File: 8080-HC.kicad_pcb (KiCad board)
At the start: 4 copper layers, 352 parts, among them U1 74HCU04, U10 74HC00, U11 74HC126, U12 74HC161, U13 74HC238, U14 74HC238, U15 74HC238, U16 74HC238, U17 74HC04, U178 74LS03, U18 74HC05, U181 74HC244, U182 74HC244, U19 74HC74, U194 74HC244, U195 74HC244, U2 74HC74, U20 74HC373, U21 74HC373, U215 74HC193, U216 74HC193, U217 74HC193, U218 74HC193, U22 74HC373, U23 74HC373, U231 74HC245, U232 74HC04, U233 74HC04, U234 74LS373, U239 74HC74, U24 74HC373, U242 74HC00, U243 74HCU04, U244 74HC00, U25 74HC244, U26 74HC244, U27 74HC244, U28 74HC244, U29 74HC244, U3 74HC00, U30 74HC373, U31 74HC373, U32 74HC244, U33 74HC244, U34 74HC244, U35 74HC244, U36 74HC373, U37 74HC373, U38 74HC244, U39 74HC244, U4 74HC04, U40 74HC244, U41 74HC244, U43 74HC04, U44 74HC04, U46 74HC04, U47 74HC04, U48 74HC04, U49 74HC04, U5 74HC00, U50 74HC04, U51 74HC04, U52 74HC04, U53 74HC238, U54 74HC238, U55 74HC238, U56 74HC238, U57 74HC04, U58 74HC04, U6 74HC04, U69 74HC05, U7 74HC05, U70 74LS05, U71 74HC04, U72 74LS126, U73 74LS126, U74 74LS126, U75 74LS126, U76 74LS126, U77 74HC00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

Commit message: place u229, u230 and D0-D7 leds
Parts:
- added U229: 74HC04, Package_DIP:DIP-14_W7.62mm, F.Cu at (-284.5, -30.5)
- added U230: 74HC04, Package_DIP:DIP-14_W7.62mm, F.Cu at (-261.6, -30.5)
- added U43: 74HC04, Package_DIP:DIP-14_W7.62mm, F.Cu at (-66.0, -45.7)
- moved L250 362.4 mm to (-249.7, -6.35), turned to 90 degrees
- moved L248 362.1 mm to (-258.8, -6.35), turned to 90 degrees
- moved L253 353.3 mm to (-236.0, -6.35), turned to 90 degrees
- moved L247 338.7 mm to (-263.4, -6.35), turned to 90 degrees
- moved L246 337.1 mm to (-268.0, -6.35), turned to 90 degrees
- moved L251 319.5 mm to (-245.1, -6.35), turned to 90 degrees
- moved B35 314.8 mm to (-236.2, -14.0), turned to 180 degrees
- moved L249 303.4 mm to (-254.3, -6.35), turned to 90 degrees
- moved L252 302.1 mm to (-240.5, -6.35), turned to 90 degrees
- renumbered D102 to L246, D100 to L247, D98 to L248, D96 to L249, D94 to L250, D92 to L251, D90 to L252, D89 to L253
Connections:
- L246 pad 1: Net-(D102-Pad1) -> Net-(L246-Pad1)
- L247 pad 1: Net-(D100-Pad1) -> Net-(L247-Pad1)
- L248 pad 1: Net-(D98-Pad1) -> Net-(L248-Pad1)
- L249 pad 1: Net-(D96-Pad1) -> Net-(L249-Pad1)
- L250 pad 1: Net-(D94-Pad1) -> Net-(L250-Pad1)
- L251 pad 1: Net-(D92-Pad1) -> Net-(L251-Pad1)
- L252 pad 1: Net-(D90-Pad1) -> Net-(L252-Pad1)
- L253 pad 1: Net-(D89-Pad1) -> Net-(L253-Pad1)
- U17 pad 10: Net-(D96-Pad1) -> (no net)
- U17 pad 11: io_D4 -> (no net)
- U17 pad 14: VCC -> (no net)
- U17 pad 5: io_D2 -> (no net)
- U17 pad 6: Net-(D92-Pad1) -> (no net)
- U17 pad 7: GND -> (no net)
- U17 pad 8: Net-(D94-Pad1) -> (no net)
- U17 pad 9: io_D3 -> (no net)
- U4 pad 1: io_D0 -> (no net)
- U4 pad 14: VCC -> (no net)
- U4 pad 2: Net-(D89-Pad1) -> (no net)
- U4 pad 3: io_D1 -> (no net)
- U4 pad 4: Net-(D90-Pad1) -> (no net)
- U4 pad 7: GND -> (no net)
- U6 pad 12: Net-(D98-Pad1) -> (no net)
- U6 pad 13: io_D5 -> (no net)

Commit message: address display leds set and half routed
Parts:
- removed the U43 at (-66.0, -45.7)
- removed the U43 at (-162.6, -295.8)
- removed U46: 74HC04, Package_DIP:DIP-14_W7.62mm
- removed the U49 at (-121.0, -302.6)
- added U228: 74HC04, Package_DIP:DIP-14_W7.62mm, F.Cu at (-312.4, -30.5)
- added U43: 74HC04, Package_DIP:DIP-14_W7.62mm, F.Cu at (-378.5, -45.0)
- added U47: 74HC04, Package_DIP:DIP-14_W7.62mm, F.Cu at (-356.8, -45.0)
- B1: renamed from RN19; value R_Network08 -> 1K
- B3: renamed from RN20; value R_Network08 -> 1K
- B33: renamed from RN16; value R_Network08 -> 2.2K
- B34: renamed from RN14; value R_Network08 -> 2.2K
- B43: renamed from RN10; value R_Network08 -> 1K
- B44: renamed from RN12; value R_Network08 -> 1K
- moved B44 436.4 mm to (-264.2, 108.7), turned to 90 degrees
- moved B43 419.1 mm to (-264.2, 83.9), turned to 90 degrees
- moved U44 385.3 mm to (-367.6, -45.0)
- moved L234 384.7 mm to (-327.4, -6.35), turned to 90 degrees
- moved L241 373.4 mm to (-294.1, -6.35), turned to 90 degrees
- moved L243 372.8 mm to (-285.0, -6.35), turned to 90 degrees
- moved L231 372.4 mm to (-341.1, -6.35), turned to 90 degrees
- moved L230 366.9 mm to (-345.7, -6.35), turned to 90 degrees
- moved L238 355.3 mm to (-307.8, -6.35), turned to 90 degrees
- moved L233 354.9 mm to (-332.0, -6.35), turned to 90 degrees
- moved L237 350.9 mm to (-313.7, -6.35), turned to 90 degrees
- moved L240 349.9 mm to (-298.7, -6.35), turned to 90 degrees
- moved L244 344.4 mm to (-280.4, -6.35), turned to 90 degrees
- moved B34 339.8 mm to (-275.8, -14.0), turned to 180 degrees
- moved L235 339.6 mm to (-322.8, -6.35), turned to 90 degrees
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- renumbered D122 to L230, D119 to L231, D116 to L232, D113 to L233, D110 to L234, D108 to L235, D106 to L236, D105 to L237, D104 to L238, D103 to L239, D101 to L240, D99 to L241, D97 to L242, D95 to L243, D93 to L244, D91 to L245, U47 to U227
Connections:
- B38 pad 2: Net-(B38-Pad2) -> (no net)
- B38 pad 3: Net-(B38-Pad3) -> (no net)
- B38 pad 4: Net-(B38-Pad4) -> (no net)
- B38 pad 5: Net-(B38-Pad5) -> (no net)
- B38 pad 8: Net-(B38-Pad8) -> (no net)
- B38 pad 9: Net-(B38-Pad9) -> (no net)
- B43 pad 2: /I/O regs/A15 -> A15
- B43 pad 3: /I/O regs/A14 -> A14
- B43 pad 4: /I/O regs/A13 -> A13
- B43 pad 5: /I/O regs/A12 -> A12
- B43 pad 6: /I/O regs/A11 -> A11
- B43 pad 7: /I/O regs/A10 -> A10
- B43 pad 8: /I/O regs/A9 -> A9
- B43 pad 9: /I/O regs/A8 -> A8
- B44 pad 2: /I/O regs/A7 -> A7
- B44 pad 3: /I/O regs/A6 -> A6
- B44 pad 4: /I/O regs/A5 -> A5
- B44 pad 5: /I/O regs/A4 -> A4
- B44 pad 6: /I/O regs/A3 -> A3
- B44 pad 7: /I/O regs/A2 -> A2
- B44 pad 8: /I/O regs/A1 -> A1
- B44 pad 9: /I/O regs/A0 -> A0
- L218 pad 1: Net-(L218-Pad1) -> (no net)
- L230 pad 1: Net-(D122-Pad1) -> Net-(L230-Pad1)
- L231 pad 1: Net-(D119-Pad1) -> Net-(L231-Pad1)
- L232 pad 1: Net-(D116-Pad1) -> Net-(L232-Pad1)
- L233 pad 1: Net-(D113-Pad1) -> Net-(L233-Pad1)
- L234 pad 1: Net-(D110-Pad1) -> Net-(L234-Pad1)
- L235 pad 1: Net-(D108-Pad1) -> Net-(L235-Pad1)
- L238 pad 1: Net-(D104-Pad1) -> Net-(L238-Pad1)
- L239 pad 1: Net-(D103-Pad1) -> Net-(L239-Pad1)
- L242 pad 1: Net-(D97-Pad1) -> Net-(L242-Pad1)
- L243 pad 1: Net-(D95-Pad1) -> Net-(L243-Pad1)
- L244 pad 1: Net-(D93-Pad1) -> Net-(L244-Pad1)
- L245 pad 1: Net-(D91-Pad1) -> Net-(L245-Pad1)
- L277 pad 1: BUSAK -> (no net)
- U10 pad 10: Net-(U10-Pad10) -> (no net)
- U10 pad 11: Net-(U10-Pad11) -> (no net)
- U10 pad 12: Net-(U10-Pad12) -> (no net)
- U10 pad 13: Net-(U10-Pad13) -> (no net)
- U10 pad 8: Net-(U10-Pad8) -> (no net)
- U10 pad 9: Net-(U10-Pad9) -> (no net)
- U11 pad 1: Net-(U11-Pad1) -> (no net)
- U11 pad 11: /Timings Generator/QC -> (no net)
- U11 pad 3: /Timings Generator/QA -> (no net)
- U11 pad 6: /Timings Generator/QB -> (no net)
- U11 pad 8: /Timings Generator/QD -> (no net)
- U12 pad 2: /Timings Generator/CLK -> (no net)
- U13 pad 10: Net-(U13-Pad10) -> (no net)
- U13 pad 11: Net-(U13-Pad11) -> (no net)
- U13 pad 12: Net-(U13-Pad12) -> (no net)
- U13 pad 13: /Timings Generator/W2 -> (no net)
- U13 pad 14: /Timings Generator/W1 -> (no net)
- U13 pad 15: /Timings Generator/W0 -> (no net)
- U13 pad 7: Net-(U13-Pad7) -> (no net)
- U13 pad 9: Net-(U13-Pad9) -> (no net)
- U14 pad 10: Net-(U14-Pad10) -> (no net)
- U14 pad 11: Net-(U14-Pad11) -> (no net)
- U14 pad 12: Net-(U14-Pad12) -> (no net)
- U14 pad 13: /Timings Generator/M2 -> (no net)
- U14 pad 14: Net-(U14-Pad14) -> (no net)
- U14 pad 15: Net-(U14-Pad15) -> (no net)
- U14 pad 7: Net-(U14-Pad7) -> (no net)
- U14 pad 9: Net-(U14-Pad9) -> (no net)
- U15 pad 10: Net-(U15-Pad10) -> (no net)
- U15 pad 11: /Timings Generator/T12 -> (no net)
- U15 pad 12: Net-(U15-Pad12) -> (no net)
- U15 pad 13: /Timings Generator/T10 -> (no net)
- U15 pad 14: /Timings Generator/T9 -> (no net)
- U15 pad 15: /Timings Generator/T8 -> (no net)
- U15 pad 7: Net-(U15-Pad7) -> (no net)
- U15 pad 9: Net-(U15-Pad9) -> (no net)
- U16 pad 10: /Timings Generator/T5 -> (no net)
- U16 pad 11: /Timings Generator/T4 -> (no net)
- U16 pad 12: /Timings Generator/T3 -> (no net)
- U16 pad 13: /Timings Generator/T2 -> (no net)
- U16 pad 14: /Timings Generator/T1 -> (no net)
- U16 pad 15: /Timings Generator/T0 -> (no net)
- U16 pad 7: /Timings Generator/T7 -> (no net)
- U16 pad 9: /Timings Generator/T6 -> (no net)
- U17 pad 1: /I/O regs/A0 -> (no net)
- U17 pad 12: Net-(U17-Pad12) -> (no net)
- U17 pad 13: Net-(U17-Pad13) -> (no net)
- U17 pad 2: Net-(D91-Pad1) -> (no net)
- U17 pad 3: /I/O regs/A1 -> (no net)
- U17 pad 4: Net-(D93-Pad1) -> (no net)
- U178 pad 4: PCCKdE -> (no net)
- U178 pad 5: T3 -> (no net)
- U18 pad 10: Net-(U18-Pad10) -> (no net)
- U18 pad 11: Net-(U18-Pad11) -> (no net)
- U18 pad 12: Net-(U18-Pad12) -> (no net)
- U18 pad 13: Net-(U18-Pad13) -> (no net)
- U18 pad 4: /regs_decode/dataOUT -> (no net)
- U18 pad 8: /regs_decode/memRD -> (no net)
- U181 pad 12: /Program Counter/A11 -> (no net)
- U181 pad 14: /Program Counter/A10 -> (no net)
- U181 pad 16: /Program Counter/A9 -> (no net)
- U181 pad 18: /Program Counter/A8 -> (no net)
- U181 pad 3: /Program Counter/A12 -> (no net)
- U181 pad 5: /Program Counter/A13 -> (no net)
- U181 pad 7: /Program Counter/A14 -> (no net)
- U181 pad 9: Net-(U181-Pad9) -> (no net)
- U182 pad 12: /Program Counter/A3 -> (no net)
- U182 pad 14: /Program Counter/A2 -> (no net)
- U182 pad 16: /Program Counter/A1 -> (no net)
- U182 pad 18: /Program Counter/A0 -> (no net)
- U182 pad 3: /Program Counter/A4 -> (no net)
- U182 pad 5: /Program Counter/A5 -> (no net)
- U182 pad 7: /Program Counter/A6 -> (no net)
- U182 pad 9: /Program Counter/A7 -> (no net)
- U19 pad 10: Net-(U19-Pad10) -> (no net)
- U19 pad 11: Net-(U19-Pad11) -> (no net)
- U19 pad 12: Net-(U19-Pad12) -> (no net)
- U19 pad 13: Net-(U19-Pad13) -> (no net)
- U19 pad 5: Net-(U19-Pad5) -> (no net)
- U19 pad 8: Net-(U19-Pad8) -> (no net)
- U19 pad 9: Net-(U19-Pad9) -> (no net)
- U2 pad 9: Net-(U2-Pad9) -> (no net)
- U20 pad 11: /regs_A_B_C_D_E/AregWR -> (no net)
- U21 pad 11: /regs_A_B_C_D_E/BregWR -> (no net)
- U215 pad 12: Net-(U215-Pad12) -> (no net)
- U215 pad 13: Net-(U215-Pad13) -> (no net)
- U216 pad 12: Net-(U216-Pad12) -> (no net)
- U217 pad 12: Net-(U217-Pad12) -> (no net)
- U218 pad 12: Net-(U218-Pad12) -> (no net)
- U22 pad 11: /regs_A_B_C_D_E/CregWR -> (no net)
- U227 pad 1: /I/O regs/A14 -> A15
- U227 pad 10: Net-(D135-Pad1) -> Net-(L233-Pad1)
- U227 pad 11: /I/O regs/d3 -> A12
- U227 pad 12: Net-(D136-Pad1) -> Net-(L231-Pad1)
- U227 pad 13: /I/O regs/d2 -> A14
- U227 pad 2: Net-(D119-Pad1) -> Net-(L230-Pad1)
- U227 pad 3: /I/O regs/A15 -> A13
- U227 pad 4: Net-(D122-Pad1) -> Net-(L232-Pad1)
- U227 pad 5: /I/O regs/s1 -> A11
- U227 pad 6: Net-(D132-Pad1) -> Net-(L234-Pad1)
- U227 pad 8: Net-(D134-Pad1) -> Net-(L235-Pad1)
- U227 pad 9: /I/O regs/s0 -> A10
- U229 pad 1: io_D6 -> A3
- U229 pad 10: (no net) -> Net-(L245-Pad1)
- U229 pad 11: (no net) -> A0
- U229 pad 12: (no net) -> Net-(L243-Pad1)
- U229 pad 13: (no net) -> A2
- U229 pad 2: Net-(L247-Pad1) -> Net-(L242-Pad1)
- U229 pad 3: io_D7 -> A1
- U229 pad 4: Net-(L246-Pad1) -> Net-(L244-Pad1)
- U229 pad 5: (no net) -> io_D7
- U229 pad 6: (no net) -> Net-(L246-Pad1)
- U229 pad 8: (no net) -> Net-(L247-Pad1)
- U229 pad 9: (no net) -> io_D6
- U23 pad 11: /regs_A_B_C_D_E/DregWR -> (no net)
- U231 pad 1: DataDIR -> (no net)
- U231 pad 19: DataG -> (no net)
- U234 pad 11: /I/O regs/T1 -> (no net)
- U24 pad 11: /regs_A_B_C_D_E/EregWR -> (no net)
- U242 pad 8: CLK -> (no net)
- U244 pad 11: CLK2 -> (no net)
- U244 pad 3: /I/O control/DataDIR -> (no net)
- U3 pad 10: /HALT/T2 -> (no net)
- U3 pad 9: /HALT/HALT -> (no net)
- U30 pad 11: /regs_HL/HregWR -> (no net)
- U31 pad 11: /regs_HL/LregWR -> (no net)
- U32 pad 12: /regs_HL/A12 -> (no net)
- U32 pad 14: /regs_HL/A13 -> (no net)
- U32 pad 16: /regs_HL/A14 -> (no net)
- U32 pad 18: /regs_HL/A15 -> (no net)
- U32 pad 3: /regs_HL/A11 -> (no net)
- U32 pad 5: /regs_HL/A10 -> (no net)
- U32 pad 7: /regs_HL/A9 -> (no net)
- U32 pad 9: /regs_HL/A8 -> (no net)
- U34 pad 12: /regs_HL/A4 -> (no net)
- U34 pad 14: /regs_HL/A5 -> (no net)
- U34 pad 16: /regs_HL/A6 -> (no net)
- U34 pad 18: /regs_HL/A7 -> (no net)
- U34 pad 3: /regs_HL/A3 -> (no net)
- U34 pad 5: /regs_HL/A2 -> (no net)
- U34 pad 7: /regs_HL/A1 -> (no net)
- U34 pad 9: /regs_HL/A0 -> (no net)
- U36 pad 11: /reg_WK/WKHregWR -> (no net)
- U37 pad 11: /reg_WK/WKLregWR -> (no net)
- U38 pad 12: /reg_WK/A12 -> (no net)
- U38 pad 14: /reg_WK/A13 -> (no net)
- U38 pad 16: /reg_WK/A14 -> (no net)
- U38 pad 18: /reg_WK/A15 -> (no net)
- U38 pad 3: /reg_WK/A11 -> (no net)
- U38 pad 5: /reg_WK/A10 -> (no net)
- U38 pad 7: /reg_WK/A9 -> (no net)
- U38 pad 9: /reg_WK/A8 -> (no net)
- U4 pad 10: Net-(U4-Pad10) -> (no net)
- U4 pad 11: Net-(U4-Pad11) -> (no net)
- U4 pad 12: Net-(U4-Pad12) -> (no net)
- U4 pad 13: Net-(U4-Pad13) -> (no net)
- U4 pad 5: Net-(U4-Pad5) -> (no net)
- U4 pad 6: Net-(U4-Pad6) -> (no net)
- U4 pad 8: Net-(U4-Pad8) -> (no net)
- U4 pad 9: Net-(U4-Pad9) -> (no net)
- U40 pad 12: /reg_WK/A4 -> (no net)
- U40 pad 14: /reg_WK/A5 -> (no net)
- U40 pad 16: /reg_WK/A6 -> (no net)
- U40 pad 18: /reg_WK/A7 -> (no net)
- U40 pad 3: /reg_WK/A3 -> (no net)
- U40 pad 5: /reg_WK/A2 -> (no net)
- U40 pad 7: /reg_WK/A1 -> (no net)
- U40 pad 9: /reg_WK/A0 -> (no net)
- U44 pad 1: /I/O regs/A6 -> (no net)
- U44 pad 10: Net-(D113-Pad1) -> (no net)
- U44 pad 11: /I/O regs/A12 -> (no net)
- U44 pad 12: Net-(D116-Pad1) -> (no net)
- U44 pad 13: /I/O regs/A13 -> (no net)
- U44 pad 2: Net-(D103-Pad1) -> (no net)
- U44 pad 3: /I/O regs/A7 -> (no net)
- U44 pad 4: Net-(D104-Pad1) -> (no net)
- U44 pad 5: /I/O regs/A10 -> (no net)
- U44 pad 6: Net-(D108-Pad1) -> (no net)
- U44 pad 8: Net-(D110-Pad1) -> (no net)
- U44 pad 9: /I/O regs/A11 -> (no net)
- U48 pad 10: /regs_decode/PCLregWR -> (no net)
- U48 pad 12: /regs_decode/SPHregWR -> (no net)
- U48 pad 8: /regs_decode/PCHregWR -> (no net)
- U52 pad 1: /regs_decode/T0 -> (no net)
- U53 pad 10: /regs_decode/LregWR -> (no net)
- U53 pad 11: /regs_decode/HregWR -> (no net)
- U53 pad 12: /regs_decode/EregWR -> (no net)
- U53 pad 13: /regs_decode/DregWR -> (no net)
- U53 pad 14: /regs_decode/CregWR -> (no net)
- U53 pad 15: /regs_decode/BregWR -> (no net)
- U53 pad 7: /regs_decode/AregWR -> (no net)
- U54 pad 14: /regs_decode/FregWR -> (no net)
- U54 pad 15: Net-(U54-Pad15) -> (no net)
- U54 pad 7: /regs_decode/WKLregWR -> (no net)
- U54 pad 9: /regs_decode/WKHregWR -> (no net)
- U55 pad 10: /regs_decode/LregRD -> (no net)
- U55 pad 11: /regs_decode/HregRD -> (no net)
- U55 pad 12: /regs_decode/EregRD -> (no net)
- U55 pad 13: /regs_decode/DregRD -> (no net)
- U55 pad 14: /regs_decode/CregRD -> (no net)
- U55 pad 15: /regs_decode/BregRD -> (no net)
- U55 pad 7: /regs_decode/AregRD -> (no net)
- U56 pad 10: /regs_decode/SPLregRD -> (no net)
- U56 pad 11: /regs_decode/SPHregRD -> (no net)
- U56 pad 12: /regs_decode/PCLregRD -> (no net)
- U56 pad 13: /regs_decode/PCHregRD -> (no net)
- U56 pad 14: /regs_decode/FregRD -> (no net)
- U56 pad 15: Net-(U56-Pad15) -> (no net)
- U56 pad 7: /regs_decode/WKLregRD -> (no net)
- U56 pad 9: /regs_decode/WKHregRD -> (no net)
- U57 pad 2: /regs_decode/SPLregWR -> (no net)
- U58 pad 3: /regs_decode/Qa -> (no net)
- U6 pad 14: Net-(U6-Pad14) -> (no net)
- U6 pad 4: /Reset/reset(inner) -> (no net)
- U6 pad 7: Net-(U6-Pad7) -> (no net)
- U69 pad 1: /I/O control/W0 -> (no net)
- U69 pad 8: /MOV / MVI/s3 -> (no net)
- U7 pad 10: /Reset/INTclr -> (no net)
- U7 pad 2: /Reset/OUTdE -> (no net)
- U7 pad 6: /Reset/HLTclr -> (no net)
- U7 pad 8: /Reset/IEFclr -> (no net)
- U77 pad 3: /I/O control/DataG -> (no net)
- U78 pad 3: /I/O control/PCADout -> (no net)
- U79 pad 1: /MOV / MVI/OP7 -> (no net)
- U8 pad 1: /BUSRQ/T3 -> (no net)
- U80 pad 11: /MOV / MVI/PCsel -> (no net)
- U82 pad 8: /MOV / MVI/HALT -> (no net)
- U83 pad 10: /MOV / MVI/T8 -> (no net)
- U83 pad 11: /MOV / MVI/d3 -> (no net)
- U83 pad 5: /MOV / MVI/T5 -> (no net)
- U83 pad 6: /MOV / MVI/PCinc -> (no net)
- U84 pad 11: /HALT/MCLR -> (no net)
- U84 pad 13: /HALT/T4 -> (no net)
- U84 pad 5: /MOV / MVI/M3 -> (no net)
- U85 pad 4: /MOV / MVI/HLTA -> (no net)
- U87 pad 11: /MOV / MVI/s2 -> (no net)
- U87 pad 3: /MOV / MVI/d2 -> (no net)
- U87 pad 6: /MOV / MVI/d1 -> (no net)
- U87 pad 8: /MOV / MVI/d0 -> (no net)
- U88 pad 3: /MOV / MVI/s1 -> (no net)
- U88 pad 6: /MOV / MVI/s0 -> (no net)
- U89 pad 8: /INR / DCR decode/LXI -> (no net)
- U9 pad 2: /BUSRQ/Mstop -> (no net)
- U9 pad 4: /BUSRQ/OUTdE -> (no net)
- U91 pad 2: /HALT/HLTclr -> (no net)
- U92 pad 1: /INR / DCR decode/OP0 -> (no net)
- U92 pad 10: /INR / DCR decode/DCR -> (no net)
- U92 pad 11: /INR / DCR decode/INR -> (no net)
- U92 pad 12: /INR / DCR decode/INX-DCX -> (no net)
- U92 pad 13: Net-(U92-Pad13) -> (no net)
- U92 pad 15: Net-(U92-Pad15) -> (no net)
- U92 pad 2: /INR / DCR decode/OP1 -> (no net)
- U92 pad 3: /INR / DCR decode/OP2 -> (no net)
- U92 pad 4: /INR / DCR decode/OP6 -> (no net)
- U92 pad 5: /INR / DCR decode/OP7 -> (no net)
- U92 pad 7: Net-(U92-Pad7) -> (no net)
- U92 pad 9: Net-(U92-Pad9) -> (no net)
- U93 pad 1: /INR / DCR decode/OP3 -> (no net)
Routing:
- net io_D6: track 0.00 -> 78.3 mm, vias 0 -> 2
- net io_D4: track 0.00 -> 76.2 mm, vias 0 -> 2
- net io_D2: track 0.00 -> 74.2 mm, vias 0 -> 2
- net io_D0: track 0.00 -> 72.2 mm, vias 0 -> 2
- net io_D7: track 0.00 -> 71.1 mm, vias 0 -> 2
- net A4: track 0.00 -> 70.6 mm, vias 0 -> 4
- net io_D5: track 0.00 -> 69.1 mm, vias 0 -> 2
- net io_D3: track 0.00 -> 67.1 mm, vias 0 -> 2
- net io_D1: track 0.00 -> 65.0 mm, vias 0 -> 2
- net A2: track 0.00 -> 54.4 mm, vias 0 -> 2
- net A0: track 0.00 -> 50.8 mm, vias 0 -> 2
- net A3: track 0.00 -> 49.3 mm, vias 0 -> 2
- net Net-(L245-Pad1): track 0.00 -> 49.0 mm, vias 0 -> 3
- net A6: track 0.00 -> 46.5 mm
- net A8: track 0.00 -> 45.8 mm
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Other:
- board text added: "Address BUS"
- board text added: "D0"
- board text added: "D1"
- board text added: "D2"
- board text added: "D3"
- board text added: "D4"
- board text added: "D5"
- board text added: "D6"
- board text added: "D7"
- board text added: "Data BUS"

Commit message: address display all routed
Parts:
- moved B44 197.5 mm to (-424.7, -6.35), turned to 270 degrees
- moved B43 196.9 mm to (-424.7, -30.2), turned to 270 degrees
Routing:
- net A0: track 50.8 -> 130.0 mm, vias 2 -> 3
- net A1: track 45.7 -> 123.4 mm, vias 2 -> 3
- net A2: track 54.4 -> 130.5 mm, vias 2 -> 3
- net A3: track 49.3 -> 123.9 mm, vias 2 -> 3
- net A4: track 70.6 -> 144.0 mm, vias 4 -> 5
- net A10: track 0.00 -> 64.7 mm, vias 0 -> 1
- net A12: track 0.00 -> 57.8 mm, vias 0 -> 1
- net A14: track 0.00 -> 50.4 mm, vias 0 -> 1
- net A11: track 0.00 -> 50.1 mm, vias 0 -> 3
- net A13: track 0.00 -> 49.1 mm, vias 0 -> 1
- net A5: track 38.0 -> 83.3 mm, vias 0 -> 1
- net Net-(L231-Pad1): track 0.00 -> 42.3 mm, vias 0 -> 2
- net A6: track 46.5 -> 87.2 mm, vias 0 -> 1
- net A15: track 0.00 -> 38.0 mm, vias 0 -> 1
- net A7: track 37.7 -> 75.6 mm, vias 0 -> 1
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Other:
- board text added: "A0"
- board text added: "A1"
- board text added: "A10"
- board text added: "A11"
- board text added: "A12"
- board text added: "A13"
- board text added: "A14"
- board text added: "A15"
- board text added: "A2"
- board text added: "A3"
- board text added: "A4"
- board text added: "A5"
- board text added: "A6"
- board text added: "A7"
- board text added: "A8"
- board text added: "A9"

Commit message: placed WKL register, start routing
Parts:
- removed U43, U44, U47: 74HC04, Package_DIP:DIP-14_W7.62mm
- added L208: LED_Small_ALT, LED_THT:LED_D3.0mm, F.Cu at (-302.3, -118.1)
- added R51: 1K, Resistor_THT:R_Axial_DIN0207_L6.3mm_D2.5mm_P10.16mm_Horizontal, F.Cu at (-315.7, -118.9)
- added R66: 1K, Resistor_THT:R_Axial_DIN0207_L6.3mm_D2.5mm_P10.16mm_Horizontal, F.Cu at (-315.7, -114.8)
- B30: renamed from RN9; value R_Network08 -> 2.2K
- R49: renamed from R19; value R -> 1K
- R50: renamed from R20; value R -> 1K
- moved L187 537.9 mm to (-415.3, -125.7)
- moved R50 528.8 mm to (-444.5, -66.0)
- moved R49 474.3 mm to (-384.8, -100.3)
- moved L203 464.6 mm to (-297.7, -61.0), turned to 90 degrees
- moved L206 456.2 mm to (-284.0, -61.0), turned to 90 degrees
- moved L204 452.8 mm to (-293.1, -61.0), turned to 90 degrees
- moved L207 450.8 mm to (-279.4, -61.0), turned to 90 degrees
- moved U193 446.3 mm to (-302.3, -71.1), turned to 90 degrees
- moved L202 439.5 mm to (-302.3, -61.0), turned to 90 degrees
- moved L200 437.2 mm to (-311.4, -61.0), turned to 90 degrees
- moved U180 430.9 mm to (-302.3, -82.5), turned to 90 degrees
- moved L205 430.6 mm to (-288.5, -61.0), turned to 90 degrees
- moved L201 430.4 mm to (-306.8, -61.0), turned to 90 degrees
- moved U214 427.4 mm to (-302.3, -45.7), turned to 90 degrees
- moved L199 425.3 mm to (-311.4, -66.0), turned to 90 degrees
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- renumbered D87 to L187, D88 to L199, D70 to L200, D72 to L201, D74 to L202, D76 to L203, D78 to L204, D80 to L205, D82 to L206, D84 to L207, U40 to U180, U41 to U193, U37 to U214
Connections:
- net /reg_WK/WKHLsel renamed WKsel
- net /reg_WK/WKHregRD renamed WKHregRD
- net /reg_WK/WKLregRD renamed WKLregRD
- U180 pad 12: (no net) -> A4
- U180 pad 14: (no net) -> A5
- U180 pad 16: (no net) -> A6
- U180 pad 18: (no net) -> A7
- U180 pad 3: (no net) -> A3
- U180 pad 5: (no net) -> A2
- U180 pad 7: (no net) -> A1
- U180 pad 9: (no net) -> A0
- U193 pad 12: /reg_WK/iB4 -> iB4
- U193 pad 14: /reg_WK/iB5 -> iB5
- U193 pad 16: /reg_WK/iB6 -> iB6
- U193 pad 18: /reg_WK/iB7 -> iB7
- U193 pad 3: /reg_WK/iB3 -> iB3
- U193 pad 5: /reg_WK/iB2 -> iB2
- U193 pad 7: /reg_WK/iB1 -> iB1
- U193 pad 9: /reg_WK/iB0 -> iB0
- U214 pad 13: /reg_WK/iB4 -> iB4
- U214 pad 14: /reg_WK/iB5 -> iB5
- U214 pad 17: /reg_WK/iB6 -> iB6
- U214 pad 18: /reg_WK/iB7 -> iB7
- U214 pad 3: /reg_WK/iB0 -> iB0
- U214 pad 4: /reg_WK/iB1 -> iB1
- U214 pad 7: /reg_WK/iB2 -> iB2
- U214 pad 8: /reg_WK/iB3 -> iB3
- U36 pad 13: /reg_WK/iB4 -> iB4
- U36 pad 14: /reg_WK/iB5 -> iB5
- U36 pad 17: /reg_WK/iB6 -> iB6
- U36 pad 18: /reg_WK/iB7 -> iB7
- U36 pad 3: /reg_WK/iB0 -> iB0
- U36 pad 4: /reg_WK/iB1 -> iB1
- U36 pad 7: /reg_WK/iB2 -> iB2
- U36 pad 8: /reg_WK/iB3 -> iB3
- U39 pad 12: /reg_WK/iB4 -> iB4
- U39 pad 14: /reg_WK/iB5 -> iB5
- U39 pad 16: /reg_WK/iB6 -> iB6
- U39 pad 18: /reg_WK/iB7 -> iB7
- U39 pad 3: /reg_WK/iB3 -> iB3
- U39 pad 5: /reg_WK/iB2 -> iB2
- U39 pad 7: /reg_WK/iB1 -> iB1
- U39 pad 9: /reg_WK/iB0 -> iB0
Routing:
- net iB4: track 227.4 -> 318.4 mm, vias 8 -> 9
- net iB5: track 255.4 -> 345.8 mm, vias 8 -> 9
- net iB7: track 238.4 -> 327.3 mm, vias 7 -> 8
- net iB0: track 248.0 -> 335.4 mm, vias 9 -> 10
- net iB1: track 252.4 -> 337.9 mm, vias 7 -> 8
- net iB3: track 250.6 -> 335.1 mm, vias 7 -> 8
- net iB2: track 252.9 -> 337.3 mm, vias 6 -> 7
- net iB6: track 282.3 -> 361.0 mm, vias 12 -> 13
- net io_D0: track 72.2 -> 105.4 mm
- net io_D7: track 71.1 -> 104.3 mm
- net io_D2: track 74.2 -> 107.3 mm
- net io_D6: track 78.3 -> 111.3 mm
- net io_D5: track 69.1 -> 102.1 mm
- net io_D4: track 76.2 -> 109.2 mm
- net io_D3: track 67.1 -> 100.1 mm
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
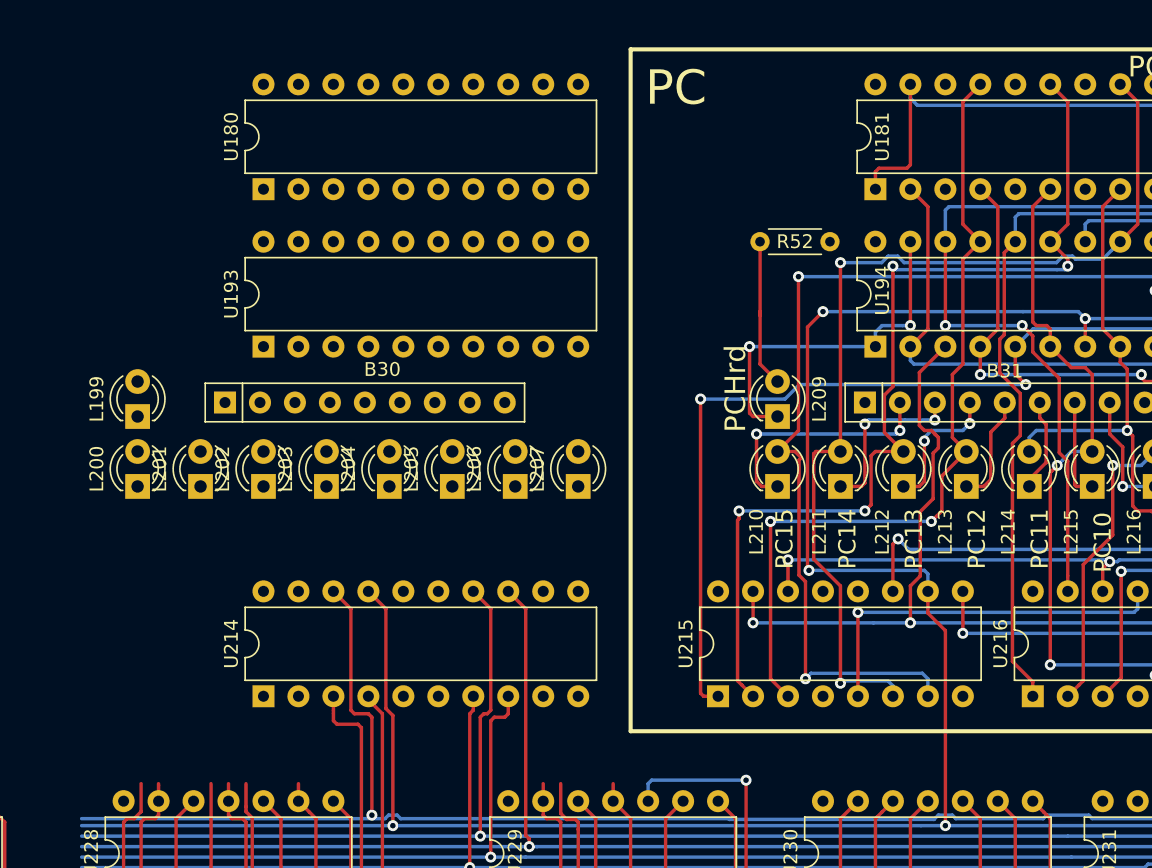
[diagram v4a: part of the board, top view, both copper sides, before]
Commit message: all WKL leds routed
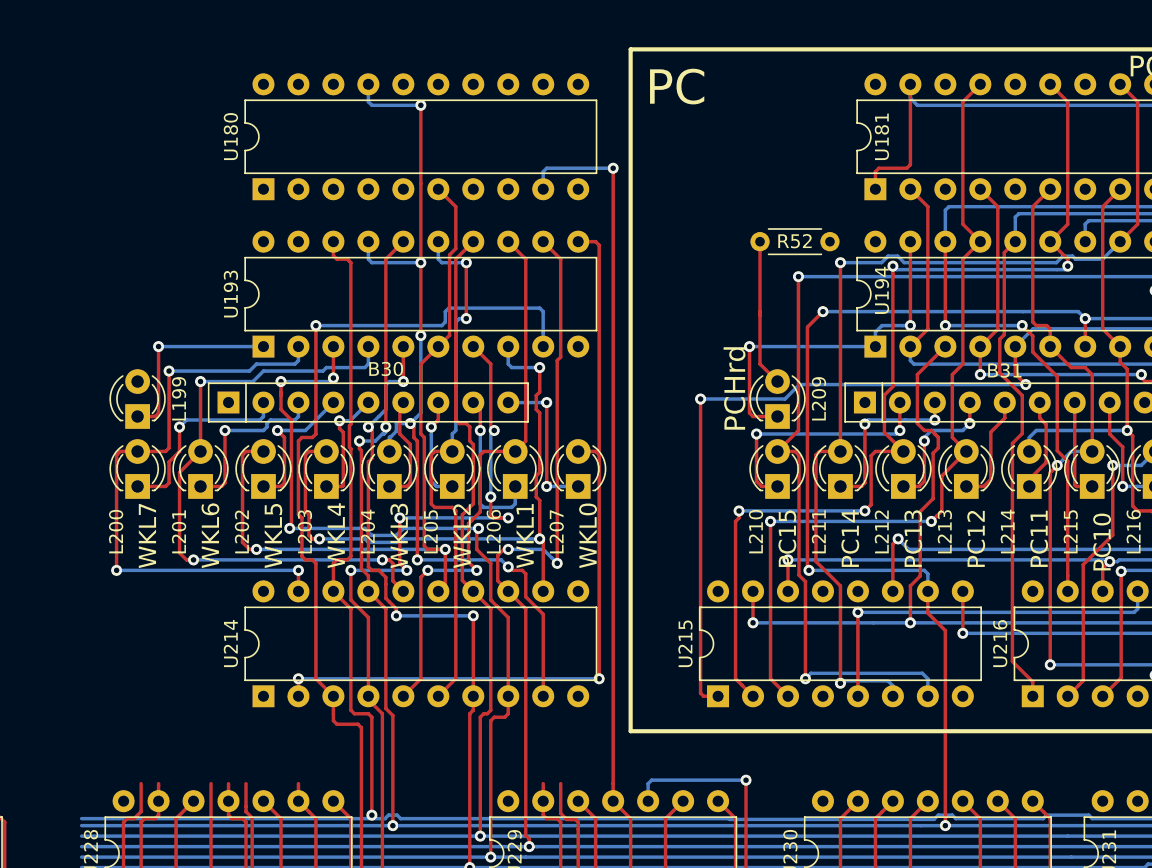
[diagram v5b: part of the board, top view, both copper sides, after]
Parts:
- moved B30 0.25 mm to (-304.8, -67.1)
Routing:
- net Net-(L204-Pad2): track 0.00 -> 64.9 mm, vias 0 -> 6
- net Net-(L207-Pad2): track 0.00 -> 57.9 mm, vias 0 -> 2
- net Net-(L202-Pad2): track 0.00 -> 55.4 mm, vias 0 -> 2
- net A0: track 131.3 -> 182.4 mm, vias 3 -> 4
- net iB0: track 335.4 -> 384.8 mm, vias 10 -> 11
- net Net-(L201-Pad2): track 0.00 -> 45.2 mm, vias 0 -> 3
- net iB3: track 335.1 -> 380.3 mm, vias 8 -> 12
- net Net-(L203-Pad2): track 0.00 -> 45.1 mm, vias 0 -> 3
- net Net-(L200-Pad2): track 0.00 -> 43.5 mm, vias 0 -> 3
- net Net-(L206-Pad2): track 0.00 -> 41.4 mm, vias 0 -> 2
- net iB1: track 337.9 -> 378.2 mm, vias 8 -> 14
- net Net-(L205-Pad2): track 0.00 -> 39.0 mm, vias 0 -> 2
- net iB2: track 337.3 -> 371.6 mm, vias 7 -> 11
- net iB4: track 318.4 -> 350.4 mm, vias 9 -> 11
- net iB6: track 361.0 -> 388.8 mm, vias 13 -> 15
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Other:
- board text added: "WKL0"
- board text added: "WKL1"
- board text added: "WKL2"
- board text added: "WKL3"
- board text added: "WKL4"
- board text added: "WKL5"
- board text added: "WKL6"
- board text added: "WKL7"
